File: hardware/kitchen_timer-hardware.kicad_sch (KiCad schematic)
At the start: 13 parts, among them J1 AVR-ISP-6, SW1 SW_Push_Open_Dual, U1 ATmega328P-A, Y1 Crystal

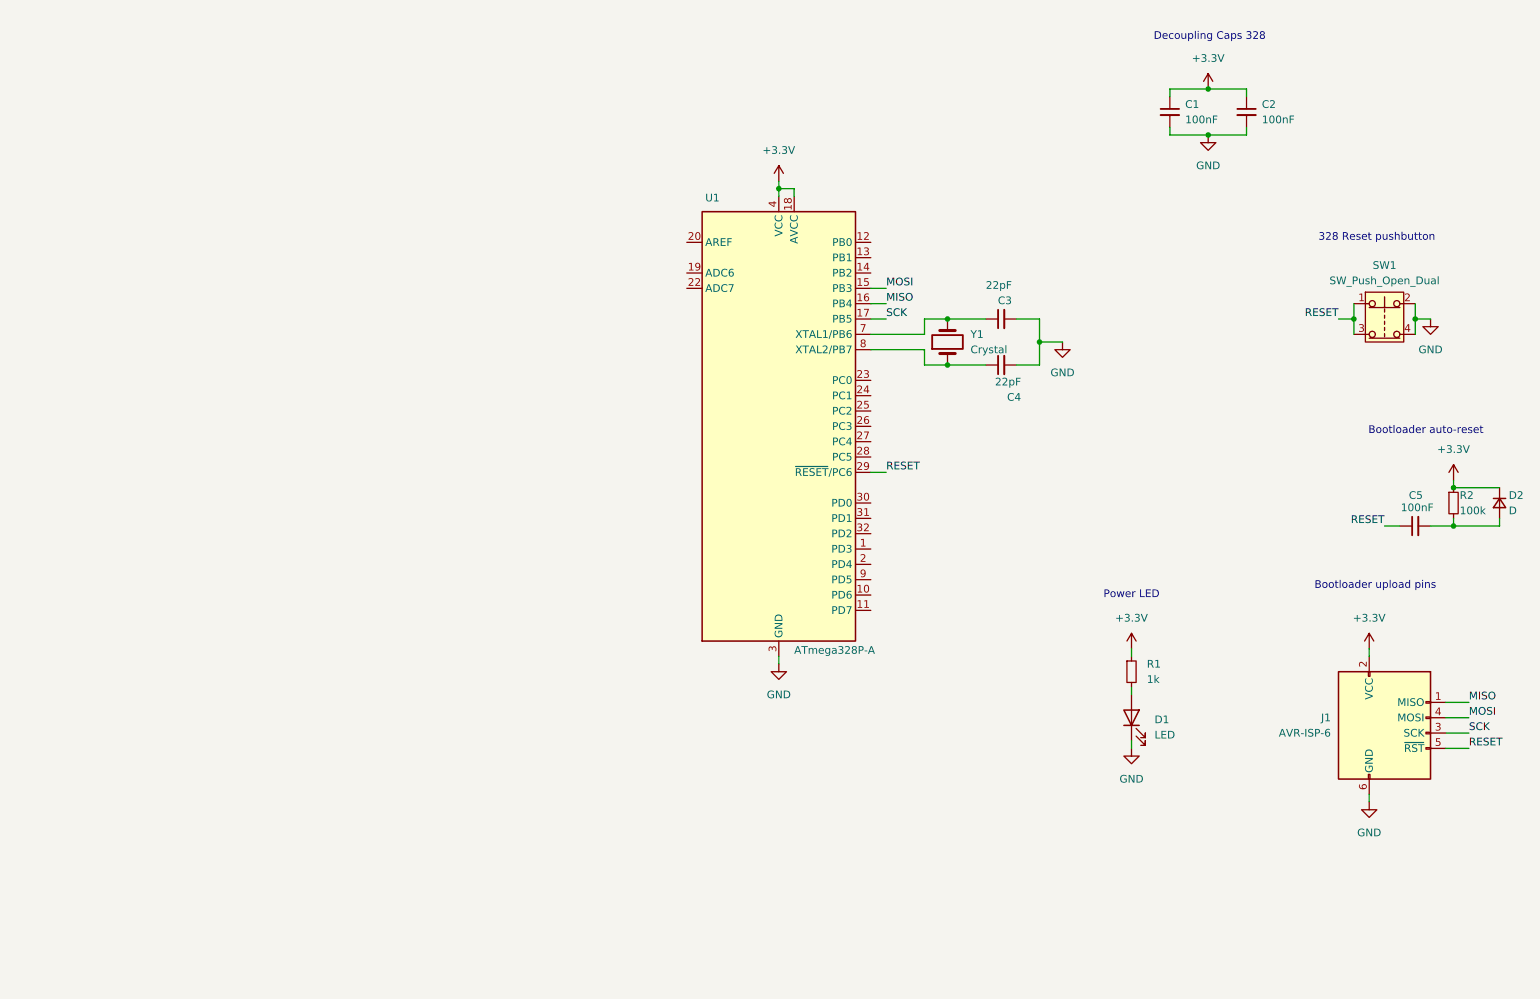
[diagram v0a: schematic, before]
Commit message: Added Bootloader auto-reset circuit.
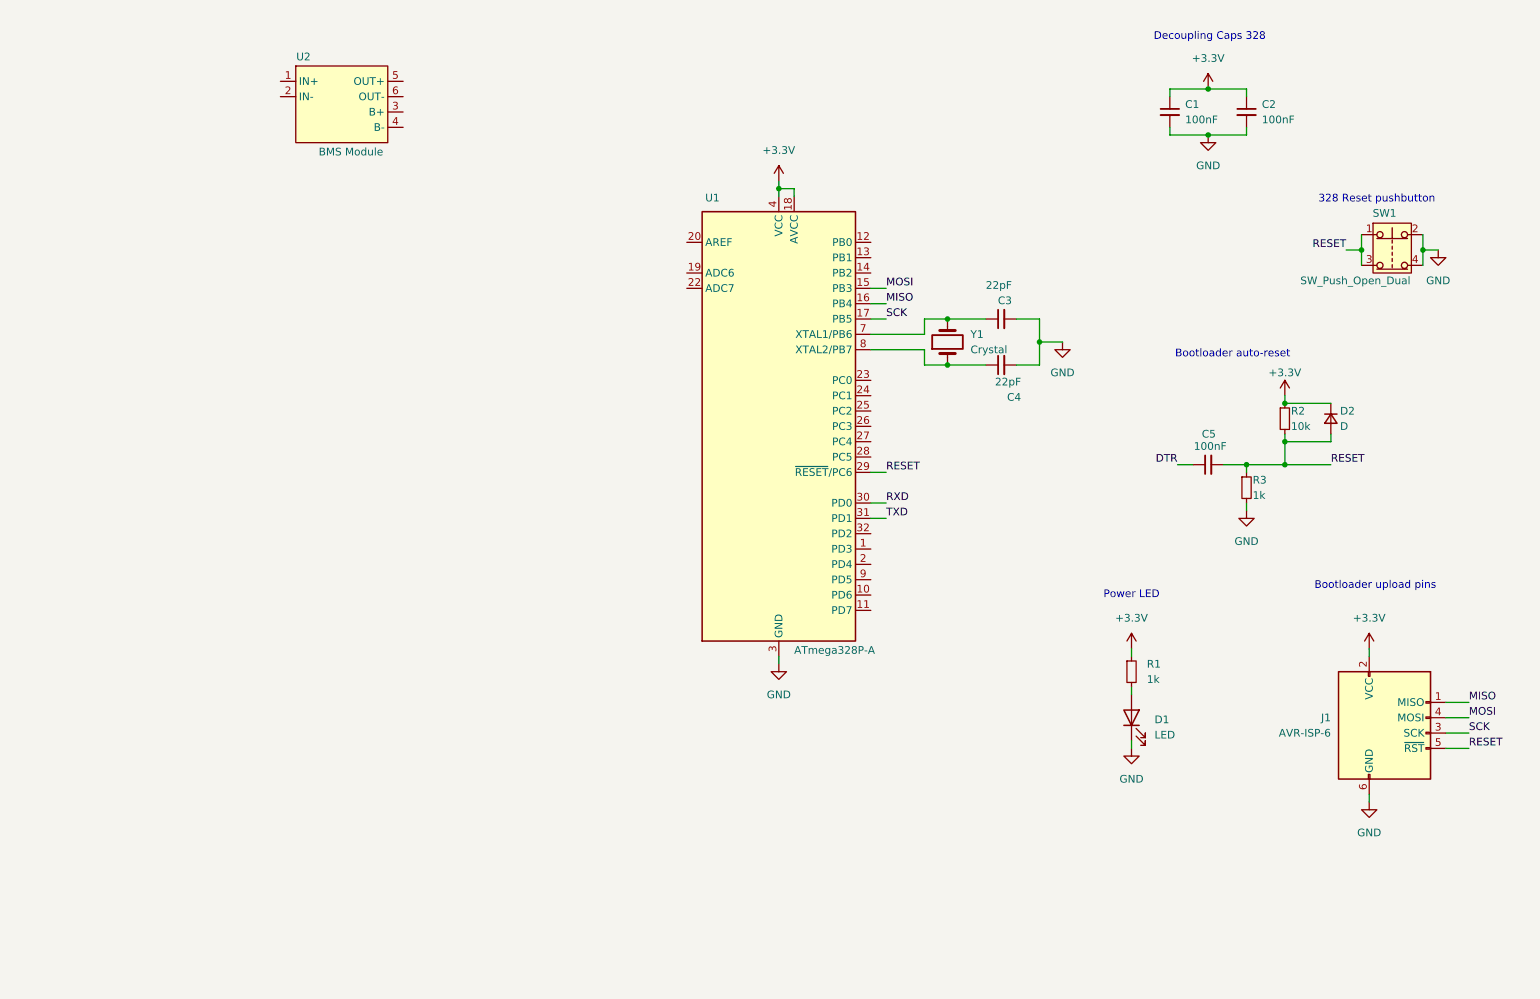
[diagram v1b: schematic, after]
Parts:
- added R3: 1k, symbol Device:R_Small
- added U2: BMS Module, symbol kitchen_timer-symbols_lib:BMS_Module
- R2: value 100k -> 10k
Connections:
- net GND: now also R3.2
- net RESET: now also C5.2, D2.2 (A), R2.2, R3.1; no longer C5.1
- net RXD: now reaches U1.30 (PD0)
- net TXD: now reaches U1.31 (PD1)
- new net DTR: C5.1
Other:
- moved on the sheet: C5, D2, R2, SW1

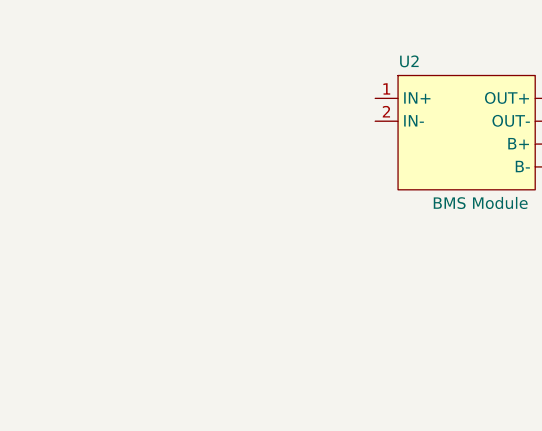
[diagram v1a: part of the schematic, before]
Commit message: Created the UART module symbol.
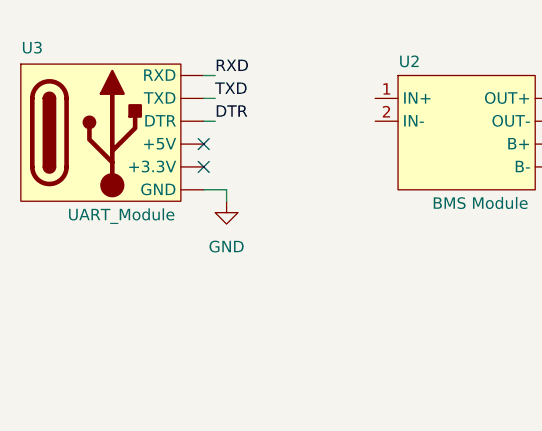
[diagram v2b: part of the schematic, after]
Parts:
- added U3: UART_Module, symbol kitchen_timer-symbols_lib:UART_Module
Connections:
- net DTR: now also U3. (TXD)
- net GND: now also U3. (TXD)
- net RXD: now also U3. (TXD)
- net TXD: now also U3. (TXD)
- no-connect marks 0 -> 2
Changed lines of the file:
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@@
 		(color 0 0 0 0)
 	)
+	(no_connect
+		(at 41.91 38.1)
+	)
+	(no_connect
+		(at 41.91 35.56)
+	)
+	(wire
+		(pts
+			(xy 44.45 40.64) (xy 44.45 41.91)
+		)
+		(stroke
+			(width 0)
+			(type default)
+		)
+	)
 	(wire
 		(pts
@@
 	(wire
 		(pts
+			(xy 41.91 40.64) (xy 44.45 40.64)
+		)
+		(stroke
+			(width 0)
+			(type default)
+		)
+	)
+	(wire
+		(pts
 			(xy 214.63 31.75) (xy 220.98 31.75)
 		)
@@
 	(wire
 		(pts
+			(xy 41.91 30.48) (xy 43.18 30.48)
+		)
+		(stroke
+			(width 0)
+			(type default)
+		)
+	)
+	(wire
+		(pts
 			(xy 227.33 90.17) (xy 227.33 88.9)
 		)
@@
 	(wire
 		(pts
+			(xy 41.91 27.94) (xy 43.18 27.94)
+		)
+		(stroke
+			(width 0)
+			(type default)
+		)
+	)
+	(wire
+		(pts
 			(xy 186.69 77.47) (xy 182.88 77.47)
 		)
@@
 		(pts
 			(xy 146.05 49.53) (xy 146.05 48.26)
+		)
+		(stroke
+			(width 0)
+			(type default)
+		)
+	)
+	(wire
+		(pts
+			(xy 41.91 33.02) (xy 43.18 33.02)
 		)
 		(stroke
@@
 		)
 	)
-	(label "RXD"
-		(at 161.29 100.33 0)
+	(label "DTR"
+		(at 43.18 33.02 0)
 		(fields_autoplaced yes)
 		(effects
@@
 		)
 	)
-	(label "MOSI"
-		(at 161.29 64.77 0)
+	(label "RXD"
+		(at 161.29 100.33 0)
 		(fields_autoplaced yes)
 		(effects
@@
 		)
 	)
+	(label "MOSI"
+		(at 161.29 64.77 0)
+		(fields_autoplaced yes)
+		(effects
+			(font
+				(size 1.27 1.27)
+			)
+			(justify left bottom)
+		)
+	)
+	(label "RXD"
+		(at 43.18 27.94 0)
+		(fields_autoplaced yes)
+		(effects
+			(font
+				(size 1.27 1.27)
+			)
+			(justify left bottom)
+		)
+	)
 	(label "TXD"
 		(at 161.29 102.87 0)
+		(fields_autoplaced yes)
+		(effects
+			(font
+				(size 1.27 1.27)
+			)
+			(justify left bottom)
+		)
+	)
+	(label "TXD"
+		(at 43.18 30.48 0)
 		(fields_autoplaced yes)
 		(effects
@@
 	)
 	(symbol
+		(lib_id "power:GND")
+		(at 44.45 41.91 0)
+		(unit 1)
+		(exclude_from_sim no)
+		(in_bom yes)
+		(on_board yes)
+		(dnp no)
+		(fields_autoplaced yes)
+		(property "Reference" "#PWR013"
+			(at 44.45 48.26 0)
+			(effects
+				(font
+					(size 1.27 1.27)
+				)
+				(hide yes)
+			)
+		)
+		(property "Value" "GND"
+			(at 44.45 46.99 0)
+			(effects
+				(font
+					(size 1.27 1.27)
+				)
+			)
+		)
+		(property "Footprint" ""
+			(at 44.45 41.91 0)
+			(effects
+				(font
+					(size 1.27 1.27)
+				)
+				(hide yes)
+			)
+		)
+		(property "Datasheet" ""
+			(at 44.45 41.91 0)
+			(effects
+				(font
+					(size 1.27 1.27)
+				)
+				(hide yes)
+			)
+		)
+		(property "Description" "Power symbol creates a global label with name \"GND\" , ground"
+			(at 44.45 41.91 0)
+			(effects
+				(font
+					(size 1.27 1.27)
+				)
+				(hide yes)
+			)
+		)
+		(pin "1"
+		)
+		(instances
+			(project "kitchen_timer-hardware"
+				(path "/8963deea-96bc-4401-b671-98fbe9ed9c6a"
+					(reference "#PWR013")
+					(unit 1)
+				)
+			)
+		)
+	)
+	(symbol
 		(lib_id "Device:C_Small")
 		(at 180.34 77.47 90)
@@
 					(unit 1)
 				)
+			)
+		)
+	)
+	(symbol
+		(lib_name "UART_Module_1")
+		(lib_id "kitchen_timer-symbols_lib:UART_Module")
+		(at 31.75 34.29 0)
+		(unit 1)
+		(exclude_from_sim no)
+		(in_bom yes)
+		(on_board yes)
+		(dnp no)
+		(property "Reference" "U3"
+			(at 22.86 24.892 0)
+			(effects
+				(font
+					(size 1.27 1.27)
+				)
+			)
+		)
+		(property "Value" "UART_Module"
+			(at 32.766 43.434 0)
+			(effects
+				(font
+					(size 1.27 1.27)
+				)
+			)
+		)
+		(property "Footprint" ""
+			(at 36.83 29.21 0)
+			(effects
+				(font
+					(size 1.27 1.27)
+				)
+				(hide yes)
+			)
+		)
+		(property "Datasheet" ""
+			(at 36.83 29.21 0)
+			(effects
+				(font
+					(size 1.27 1.27)
+				)
+				(hide yes)
+			)
+		)
+		(property "Description" ""
+			(at 36.83 29.21 0)
+			(effects
+				(font
+					(size 1.27 1.27)
+				)
+				(hide yes)
+			)
+		)
+		(pin ""
+		)
+		(pin ""
+		)
+		(pin ""
+		)
+		(pin ""
+		)
+		(pin ""
+		)
+		(pin ""
+		)
+		(instances
+			(project "kitchen_timer-hardware"
+				(path "/8963deea-96bc-4401-b671-98fbe9ed9c6a"
+					(reference "U3")
+					(unit 1)
+				)

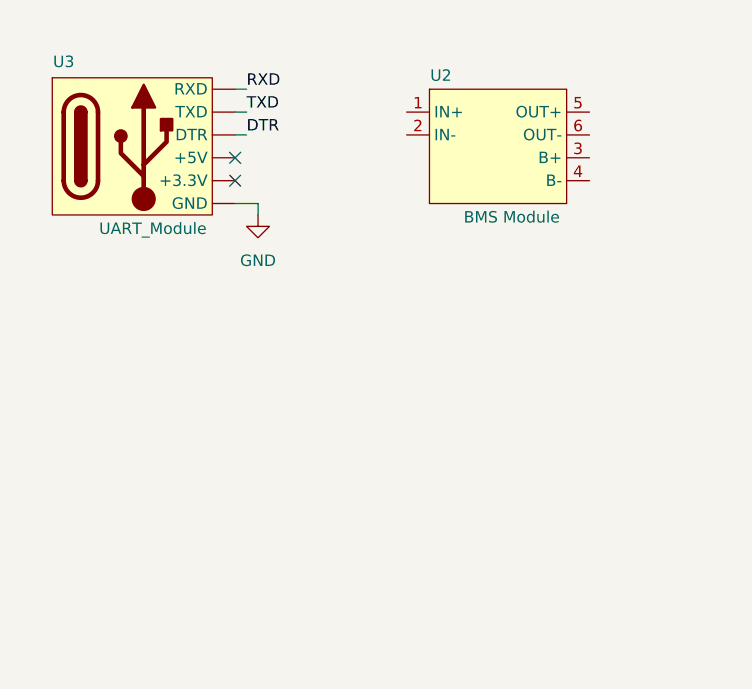
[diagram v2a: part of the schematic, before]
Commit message: Completed UART Module section and schematic.
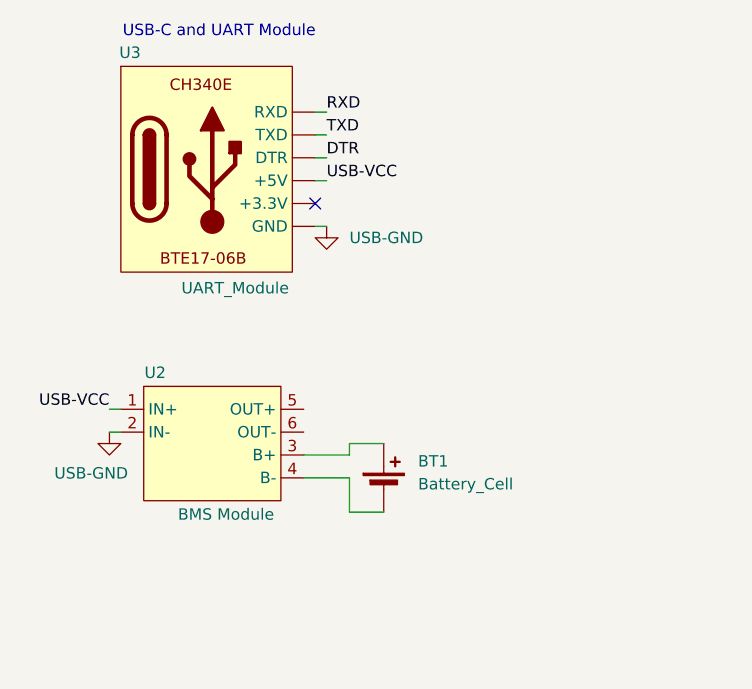
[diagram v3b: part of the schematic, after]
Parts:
- added BT1: Battery_Cell, symbol Device:Battery_Cell
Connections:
- net GND: no longer U3. (TXD)
- net USB-VCC: now reaches U2.1 (IN+)
- net USB-VCC: now also U3. (TXD)
- net USB-GND: now reaches U2.2 (IN-)
- net USB-GND: now also U3. (TXD)
- net at U2.3 (B+): now also BT1.1 (+)
- net at U2.4 (B-): now also BT1.2 (-)
- no-connect marks 2 -> 1
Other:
- note added: "USB-C and UART Module"
- moved on the sheet: U2

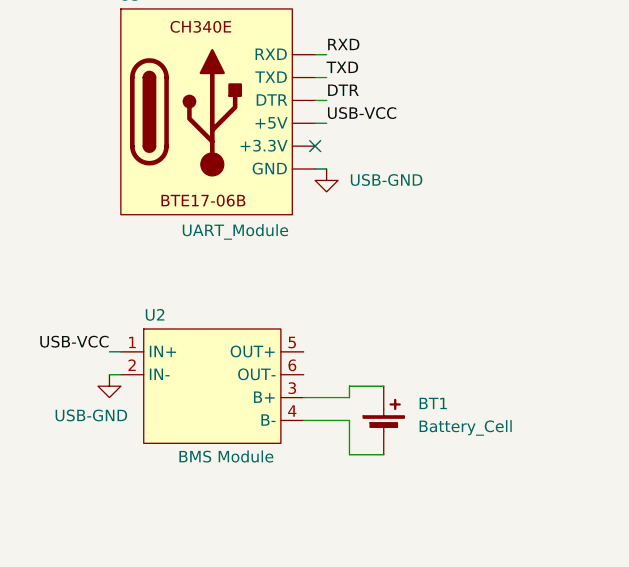
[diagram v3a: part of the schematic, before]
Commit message: Added a lable to the BMS
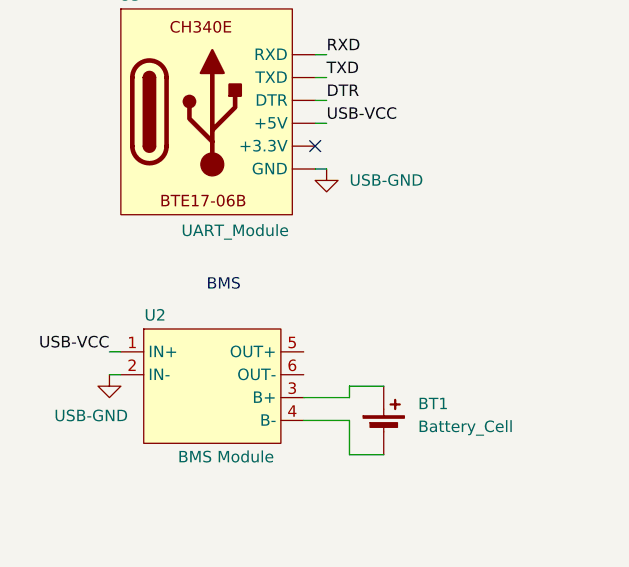
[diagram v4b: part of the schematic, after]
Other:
- note added: "BMS"
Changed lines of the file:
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@@
+		)
+	)
+	(text "BMS"
+		(exclude_from_sim no)
+		(at 40.64 56.134 0)
+		(effects
+			(font
+				(size 1.27 1.27)
+			)
 		)
 	)

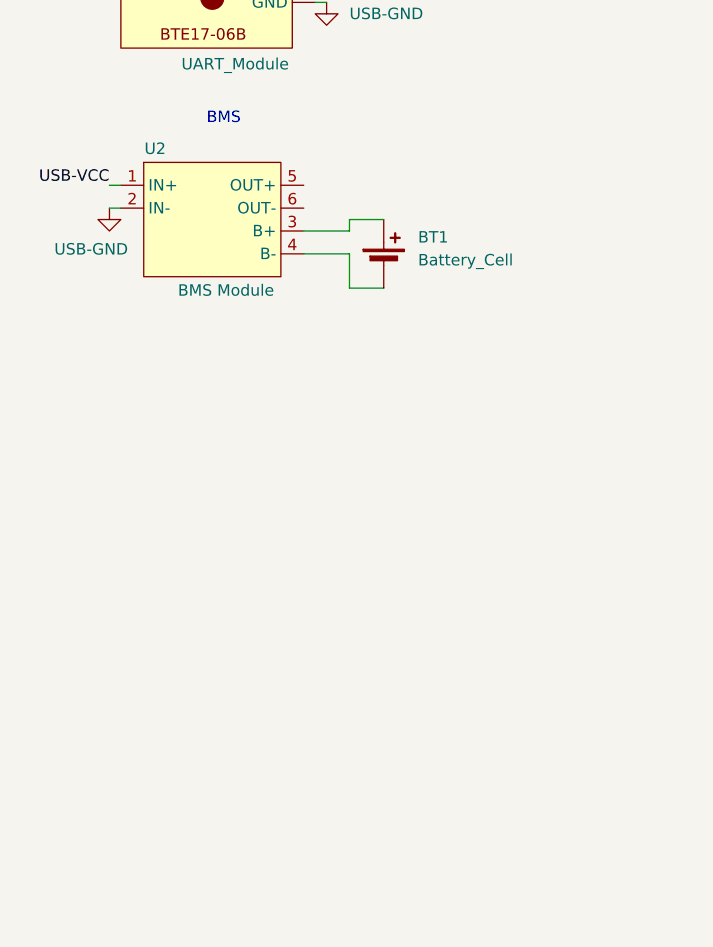
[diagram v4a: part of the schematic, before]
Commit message: Added the 3.3V Resulator schematic
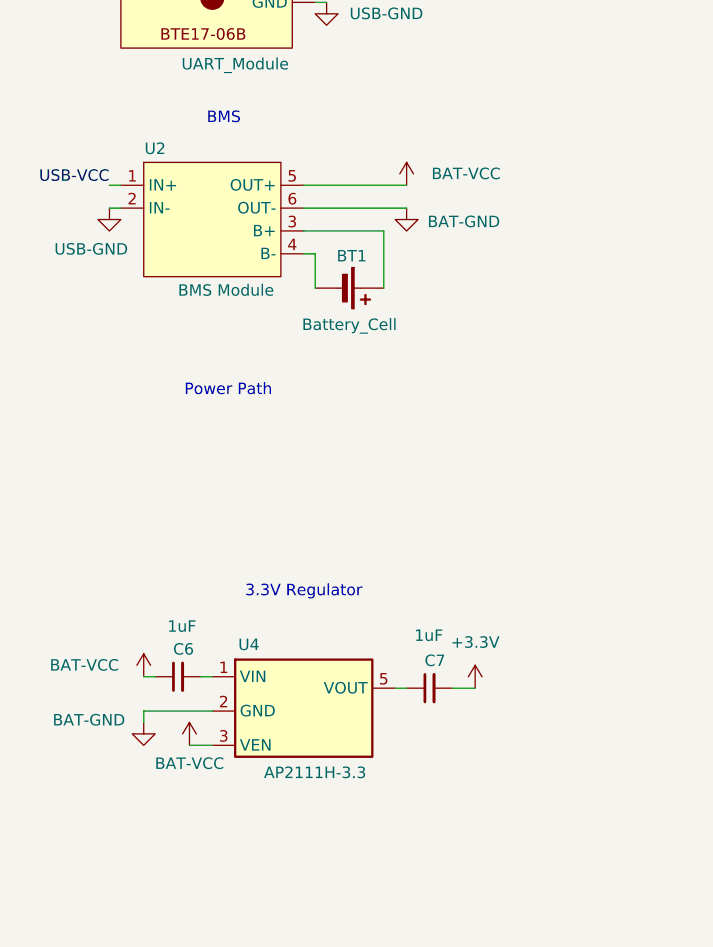
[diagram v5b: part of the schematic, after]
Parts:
- added C6, C7: 1uF, symbol Device:C_Small
- added U4: AP2111H-3.3, symbol kitchen_timer-symbols_lib:AP2111H-3.3TRG1
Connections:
- net +3.3V: now also C7.2
- net BAT-VCC: now reaches U2.5 (OUT+)
- net BAT-VCC: now also C6.1, U4.3 (VEN)
- net BAT-GND: now reaches U2.6 (OUT-)
- net BAT-GND: now also U4.2 (GND)
- new net: C6.2, U4.1 (VIN)
- new net: C7.1, U4.5 (VOUT)
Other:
- note added: "3.3V Regulator"
- note added: "Power Path"
- moved on the sheet: BT1
